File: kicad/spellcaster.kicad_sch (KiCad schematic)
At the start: 38 parts, among them SW1 SW_Push, SW2 SW_Push, U1 nRF52820-QDxx, Y1 32k, Y2 Crystal_GND24

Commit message: Initial routing
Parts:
- removed H3, H4: MountingHole, MountingHole:MountingHole_2.2mm_M2_Pad_Via, symbol Mechanical:MountingHole
- removed SW1, SW2: SW_Push, Button_Switch_SMD:SW_SPST_PTS645, symbol Switch:SW_Push
- added C14, C16: 100n, Capacitor_SMD:C_0402_1005Metric, symbol Device:C_Small
- added R2, R3: 10k, Resistor_SMD:R_0402_1005Metric, symbol Device:R_Small
- added S2: B3U-1000P, Snapeda:SW_B3U-1000P, symbol Snapeda:B3U-1000P
- added U2: LSM6DSL, Package_LGA:LGA-14_3x2.5mm_P0.5mm_LayoutBorder3x4y, symbol Sensor_Motion:LSM6DSL
- BT1: footprint Battery:BatteryHolder_Keystone_3002_1x2032 -> Connector_Wire:SolderWire-0.5sqmm_1x02_P4.8mm_D0.9mm_OD2.3mm
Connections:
- net BTN_A: now also S2.2
- net GND: now also C14.1, C16.1, S2.1, U2.1 (SDO/SA0), U2.2 (SDX), U2.3 (SCX), U2.6 (GND), U2.7 (GND)
- net GPIO: no longer U1.7 (P0.07)
- net VDD: now also R2.2, R3.2, U2.12 (CS)
- net SDA: now reaches U1.14 (P0.14)
- net SDA: now also R2.1, U2.14 (SDA)
- net SCL: now reaches U1.15 (P0.15)
- net SCL: now also R3.1, U2.13 (SCL)
- net INT2: now reaches U1.6 (P0.06)
- net INT2: now also U2.9 (INT2)
- net BTN_B: no longer names the net of U1.36 (AIN0/P0.02)
- new net: C16.2, U2.8 (VDD)
- new net: C14.2, U2.5 (VDDIO)
- new net INT1: U1.7 (P0.07), U2.4 (INT1)
- no-connect marks 15 -> 13
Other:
- moved on the sheet: BT1, C1, C10, C12, C9, H1, H2, S1, TP1, TP2, TP3, TP4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

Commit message: Silkscreen + stitching
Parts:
- removed H1: MountingHole, MountingHole:MountingHole_2.2mm_M2_Pad_Via, symbol Mechanical:MountingHole
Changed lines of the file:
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@@
-    )
-  )
-  (symbol (lib_id "Mechanical:MountingHole") (at 256.54 17.78 0) (unit 1)
-    (in_bom no) (on_board yes) (dnp no) (fields_autoplaced)
-    (property "Reference" "H1" (at 259.08 17.145 0)
-      (effects (font (size 1.27 1.27)) (justify left))
-    )
-    (property "Value" "MountingHole" (at 259.08 19.685 0)
-      (effects (font (size 1.27 1.27)) (justify left))
-    )
-    (property "Footprint" "MountingHole:MountingHole_2.2mm_M2_Pad_Via" (at 256.54 17.78 0)
-      (effects (font (size 1.27 1.27)) hide)
-    )
-    (property "Datasheet" "~" (at 256.54 17.78 0)
-      (effects (font (size 1.27 1.27)) hide)
-    )
-    (instances
-      (project "spellcaster"
-        (path "/bca210d0-b1b0-44be-885f-55d81883bdbb"
-          (reference "H1") (unit 1)
-        )
-      )
     )
   )

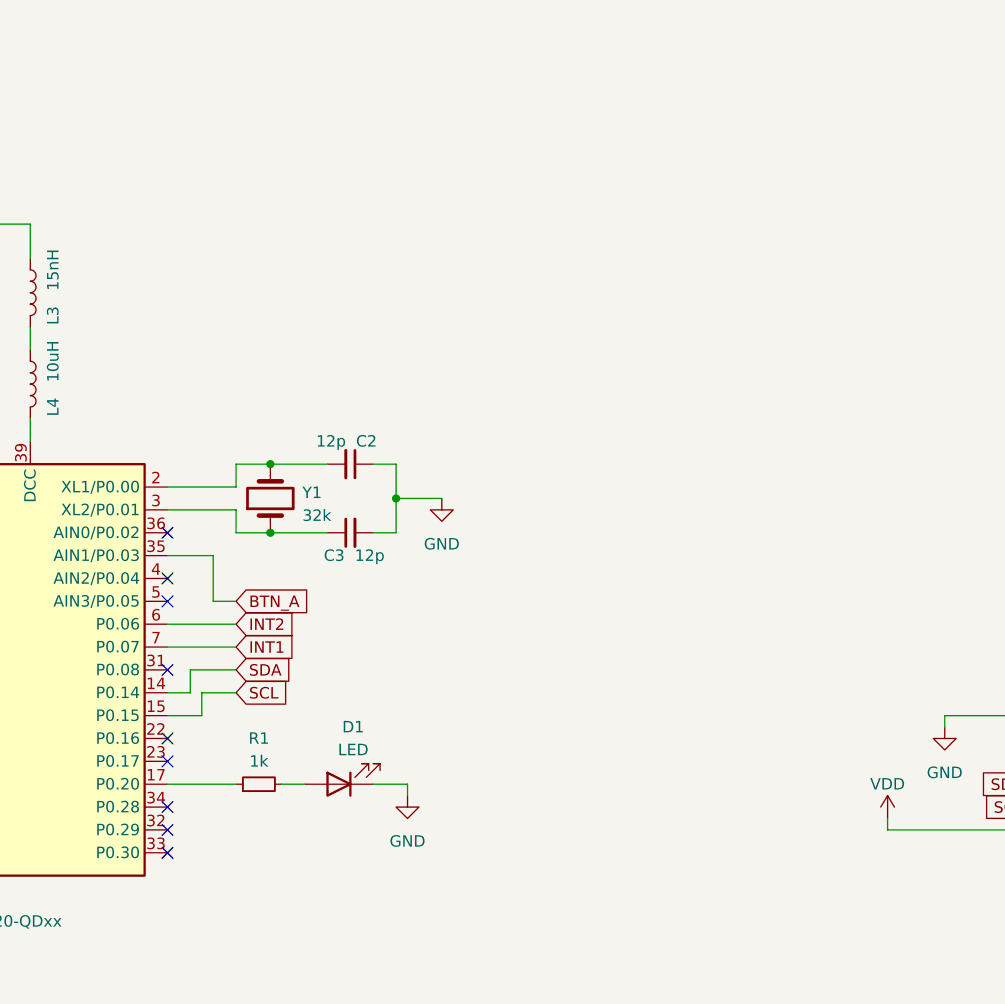
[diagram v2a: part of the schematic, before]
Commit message: Add vibration motor
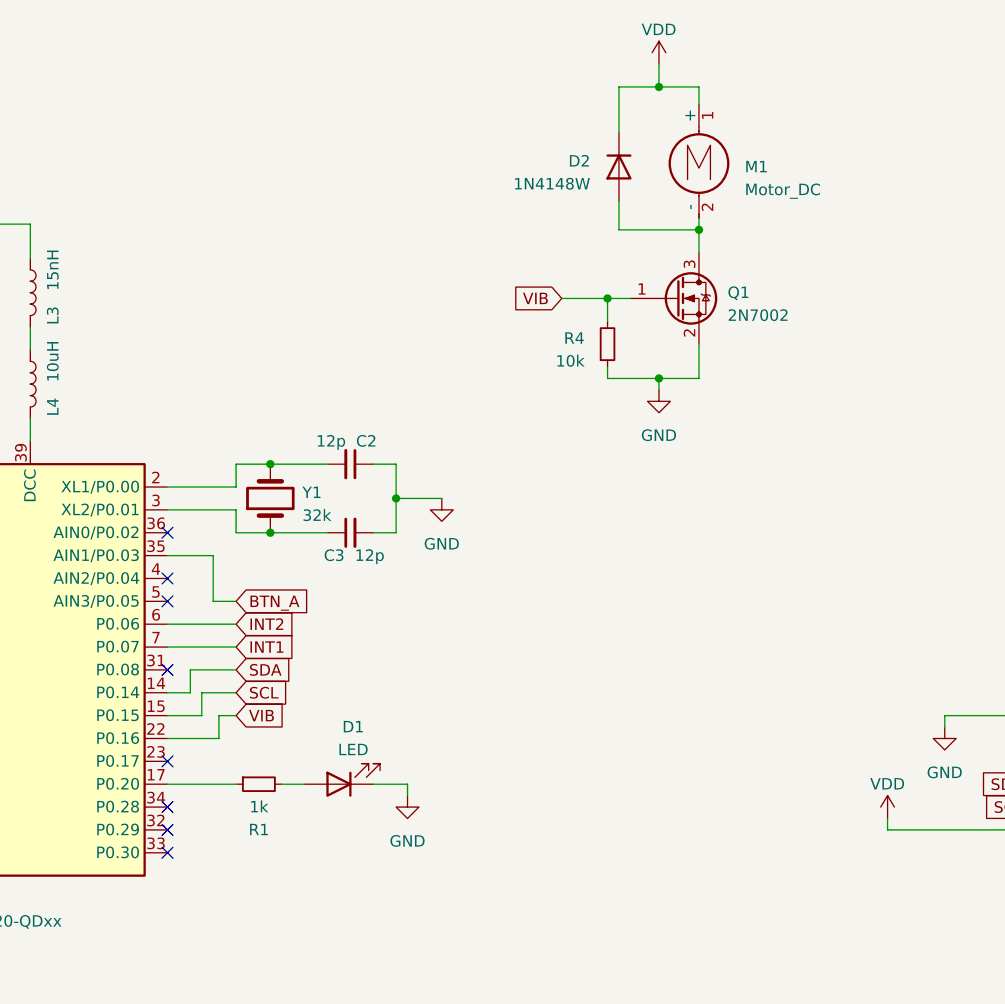
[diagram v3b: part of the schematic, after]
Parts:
- added D2: 1N4148W, Diode_SMD:D_SOD-123, symbol Diode:1N4148W
- added M1: Motor_DC, TestPoint:TestPoint_2Pads_Pitch2.54mm_Drill0.8mm, symbol Motor:Motor_DC
- added Q1: 2N7002, Package_TO_SOT_SMD:SOT-23, symbol Transistor_FET:2N7002
- added R4: 10k, Resistor_SMD:R_0402_1005Metric, symbol Device:R_Small
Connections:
- net GND: now also Q1.2 (S), R4.1
- net VDD: now also D2.1 (K), M1.1 (+)
- net VIB: now reaches U1.22 (P0.16)
- net VIB: now also Q1.1 (G), R4.2
- new net: D2.2 (A), M1.2 (-), Q1.3 (D)
- no-connect marks 13 -> 12

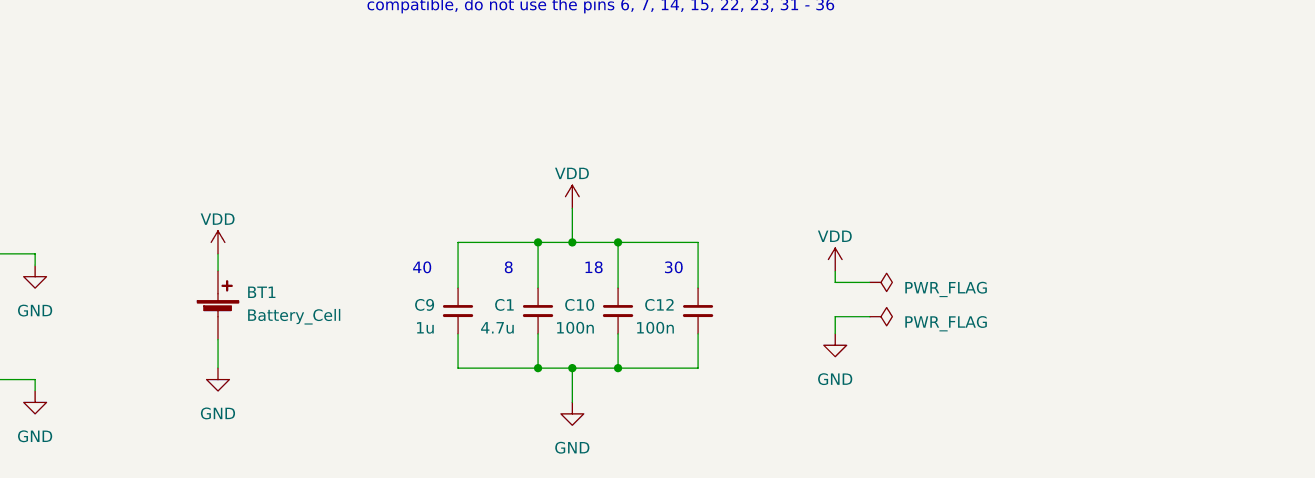
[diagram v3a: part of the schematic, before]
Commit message: Add optional CR2032 holder
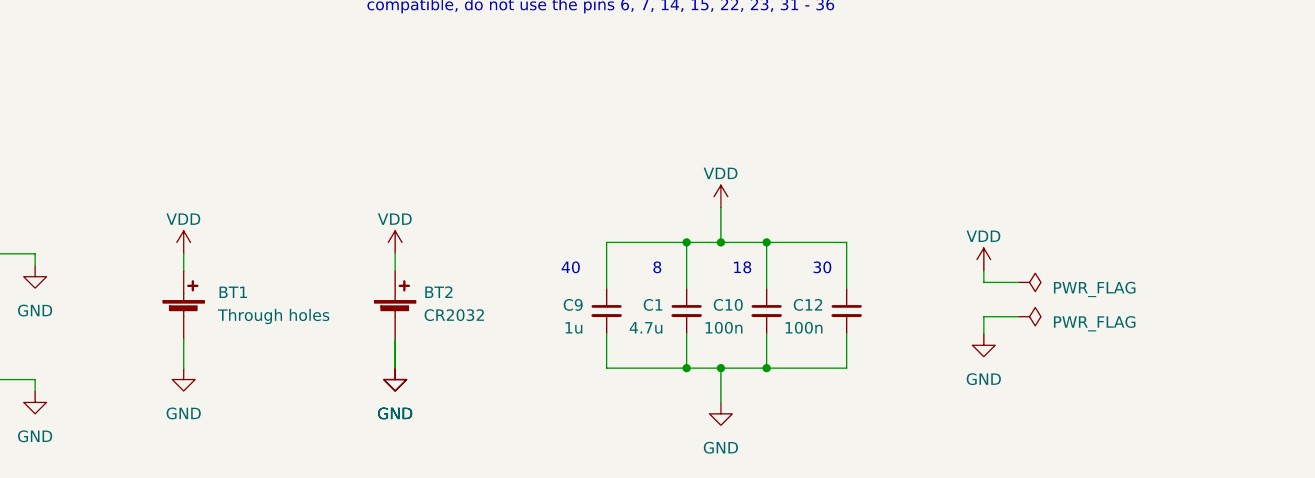
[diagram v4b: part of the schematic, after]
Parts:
- added BT2: CR2032, Battery:BatteryHolder_Keystone_1060_1x2032, symbol Device:Battery_Cell
- BT1: value Battery_Cell -> Through holes
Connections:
- net GND: now also BT2.2 (-)
- net VDD: now also BT2.1 (+)
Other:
- moved on the sheet: BT1, C1, C10, C12, C9

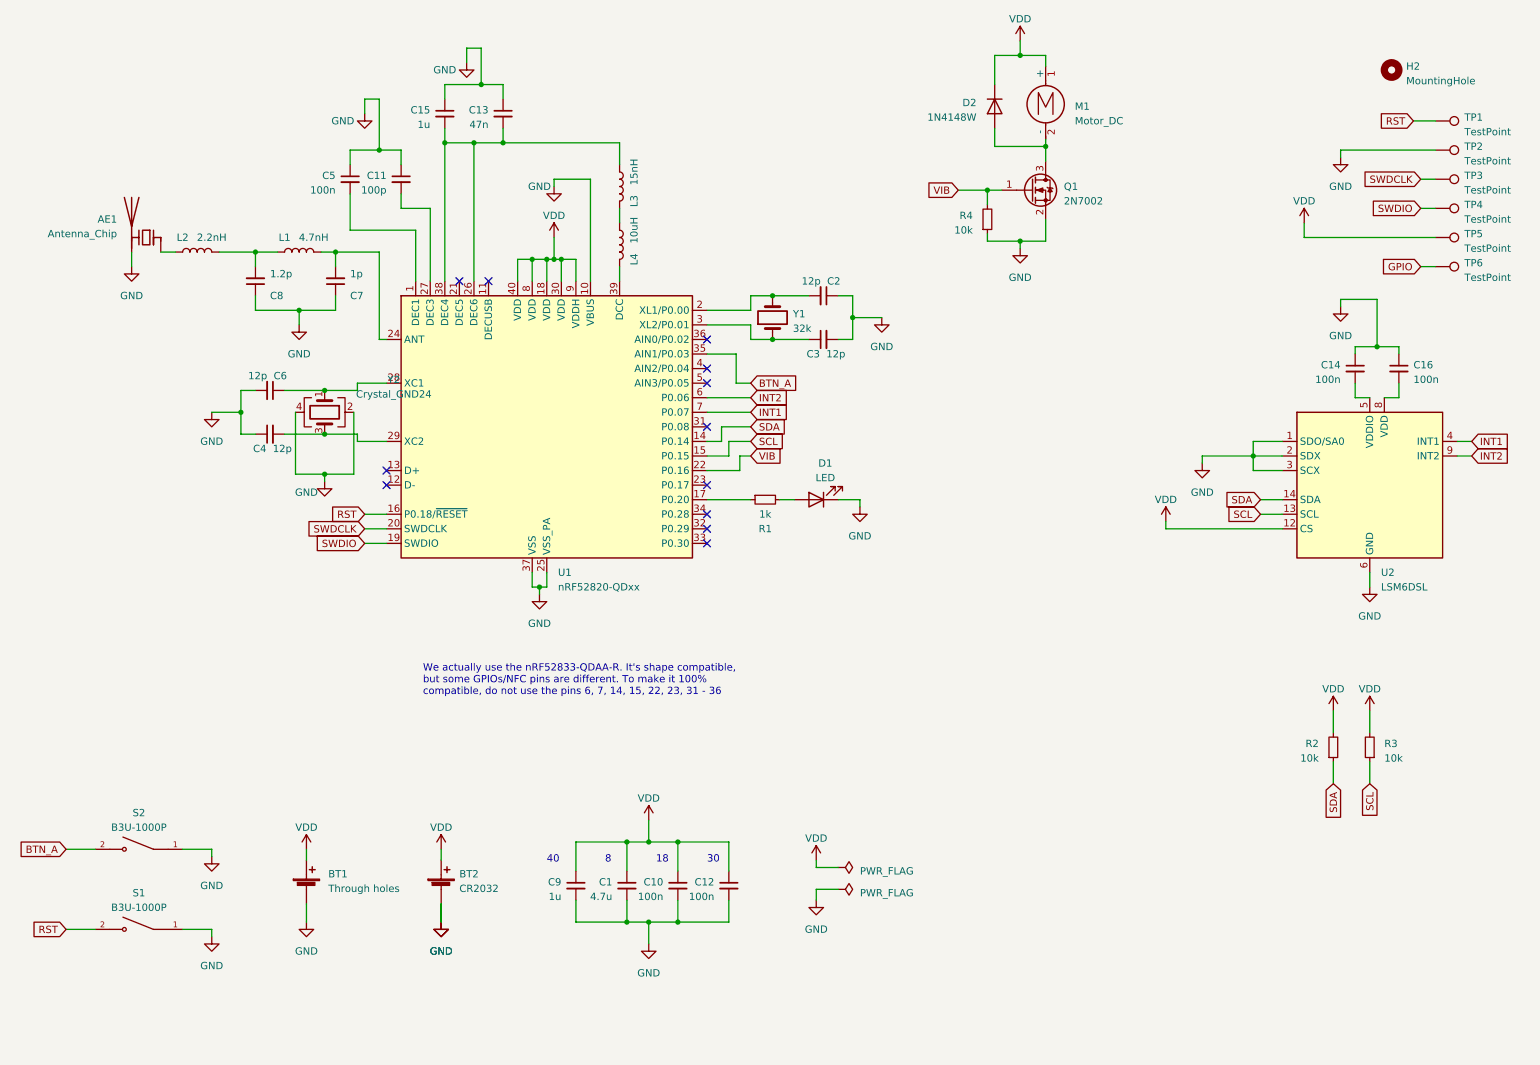
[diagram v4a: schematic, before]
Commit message: Fixed missing accel vcc connection
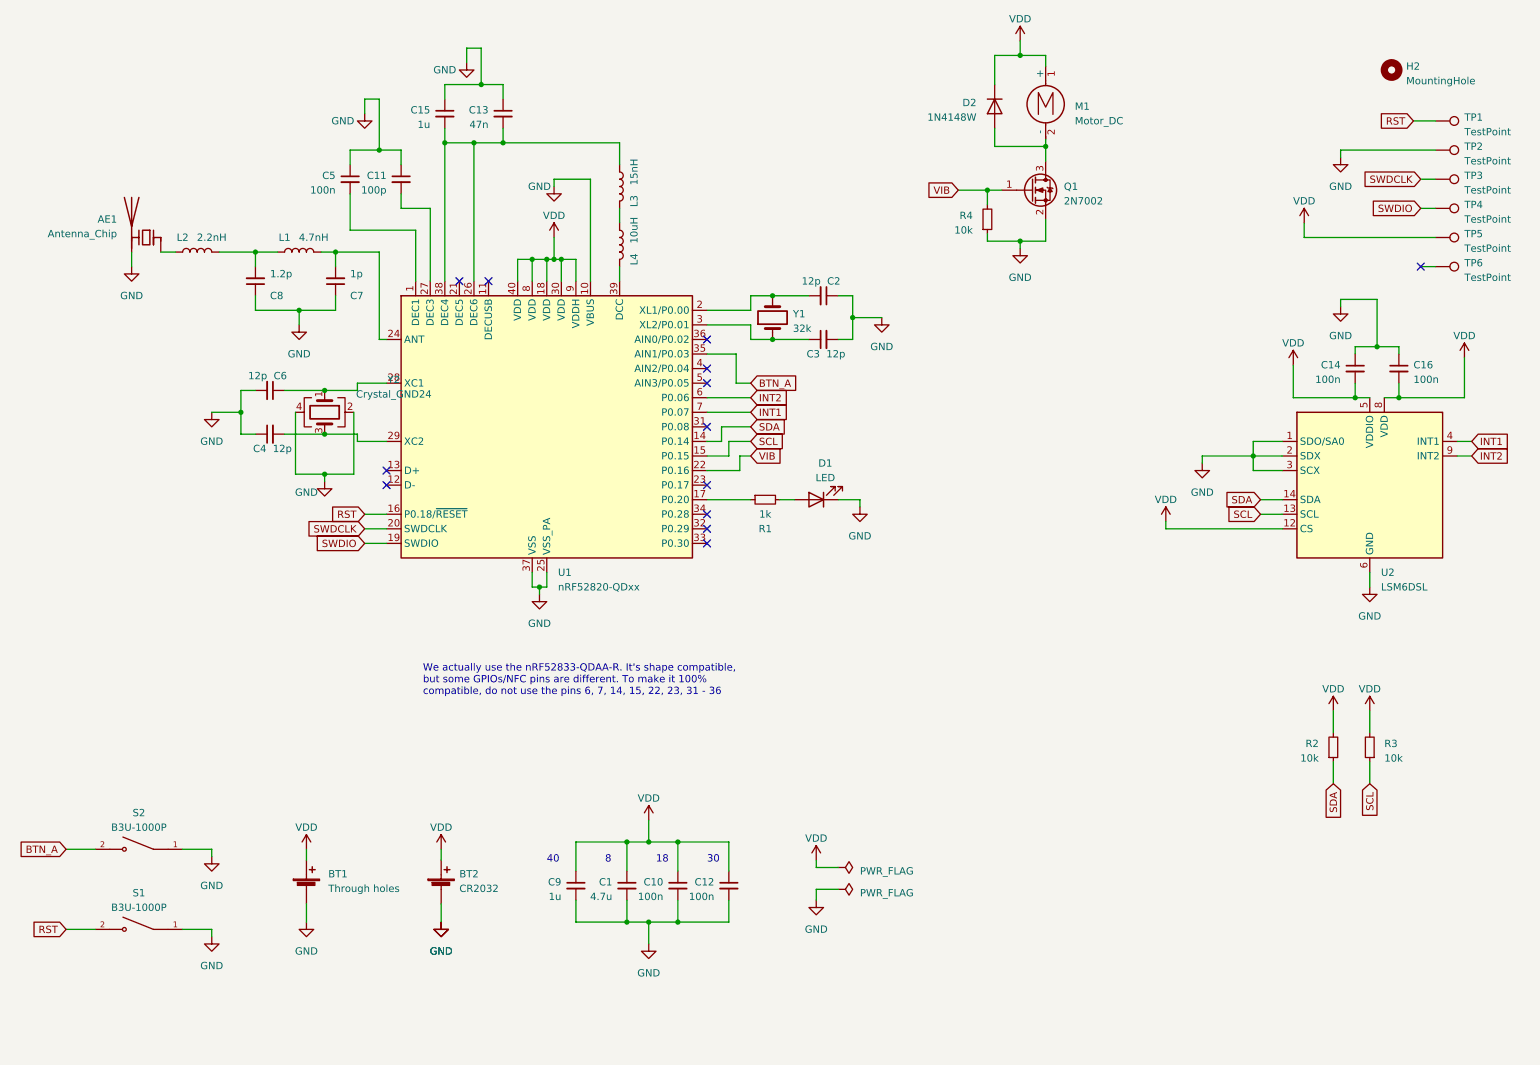
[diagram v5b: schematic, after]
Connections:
- net VDD: now also C14.2, C16.2, U2.5 (VDDIO), U2.8 (VDD)
- net GPIO: no longer names the net of TP6.1
- no-connect marks 12 -> 13
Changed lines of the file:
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@@
   (junction (at 148.59 63.5) (diameter 0) (color 0 0 0 0)
   )
+  (junction (at 250.19 81.28) (diameter 0) (color 0 0 0 0)
+  )
   (junction (at 106.68 57.15) (diameter 0) (color 0 0 0 0)
   )
@@
   (junction (at 254 72.39) (diameter 0) (color 0 0 0 0)
   )
+  (junction (at 257.81 81.28) (diameter 0) (color 0 0 0 0)
+  )
+  (no_connect (at 261.62 58.42))
   (no_connect (at 137.16 78.74))
   (no_connect (at 137.16 104.14))
@@
     (stroke (width 0) (type default))
   )
+  (wire (pts (xy 257.81 81.28) (xy 269.24 81.28))
+    (stroke (width 0) (type default))
+  )
   (wire (pts (xy 148.59 71.12) (xy 154.94 71.12))
     (stroke (width 0) (type default))
@@
     (stroke (width 0) (type default))
   )
+  (wire (pts (xy 239.395 81.28) (xy 250.19 81.28))
+    (stroke (width 0) (type default))
+  )
   (wire (pts (xy 132.08 168.91) (xy 132.08 172.72))
     (stroke (width 0) (type default))
@@
     (stroke (width 0) (type default))
   )
+  (wire (pts (xy 269.24 74.295) (xy 269.24 81.28))
+    (stroke (width 0) (type default))
+  )
   (wire (pts (xy 80.01 71.12) (xy 81.28 71.12))
     (stroke (width 0) (type default))
@@
     (stroke (width 0) (type default))
   )
+  (wire (pts (xy 239.395 75.565) (xy 239.395 81.28))
+    (stroke (width 0) (type default))
+  )
   (wire (pts (xy 77.47 101.6) (xy 81.28 101.6))
     (stroke (width 0) (type default))
   )
   (wire (pts (xy 196.215 50.165) (xy 196.215 53.975))
-    (stroke (width 0) (type default))
-  )
-  (wire (pts (xy 90.805 169.545) (xy 90.805 172.72))
     (stroke (width 0) (type default))
   )
@@
     )
   )
-  (global_label "GPIO" (shape input) (at 261.62 58.42 180) (fields_autoplaced)
-    (effects (font (size 1.27 1.27)) (justify right))
-    (property "Intersheetrefs" "${INTERSHEET_REFS}" (at 254.2389 58.42 0)
-      (effects (font (size 1.27 1.27)) (justify right) hide)
-    )
-  )
   (global_label "VIB" (shape input) (at 180.975 45.085 180) (fields_autoplaced)
     (effects (font (size 1.27 1.27)) (justify right))
@@
         (path "/bca210d0-b1b0-44be-885f-55d81883bdbb"
           (reference "#PWR01") (unit 1)
+        )
+      )
+    )
+  )
+  (symbol (lib_id "power:VDD") (at 239.395 75.565 0) (unit 1)
+    (in_bom yes) (on_board yes) (dnp no) (fields_autoplaced)
+    (property "Reference" "#PWR033" (at 239.395 79.375 0)
+      (effects (font (size 1.27 1.27)) hide)
+    )
+    (property "Value" "VDD" (at 239.395 71.755 0)
+      (effects (font (size 1.27 1.27)))
+    )
+    (property "Footprint" "" (at 239.395 75.565 0)
+      (effects (font (size 1.27 1.27)) hide)
+    )
+    (property "Datasheet" "" (at 239.395 75.565 0)
+      (effects (font (size 1.27 1.27)) hide)
+    )
+    (pin "1")
+    (instances
+      (project "spellcaster"
+        (path "/bca210d0-b1b0-44be-885f-55d81883bdbb"
+          (reference "#PWR033") (unit 1)
         )
       )
@@
         )
       )
+    )
+  )
+  (symbol (lib_id "power:VDD") (at 269.24 74.295 0) (unit 1)
+    (in_bom yes) (on_board yes) (dnp no) (fields_autoplaced)
+    (property "Reference" "#PWR034" (at 269.24 78.105 0)
+      (effects (font (size 1.27 1.27)) hide)
+    )
+    (property "Value" "VDD" (at 269.24 70.485 0)
+      (effects (font (size 1.27 1.27)))
+    )
+    (property "Footprint" "" (at 269.24 74.295 0)
+      (effects (font (size 1.27 1.27)) hide)
+    )
+    (property "Datasheet" "" (at 269.24 74.295 0)
+      (effects (font (size 1.27 1.27)) hide)
+    )
+    (pin "1")
+    (instances
+      (project "spellcaster"
+        (path "/bca210d0-b1b0-44be-885f-55d81883bdbb"
+          (reference "#PWR034") (unit 1)
+        )
+      )

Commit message: Plotted and ordered
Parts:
- M1: now left out of the parts list
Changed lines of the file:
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@@
   )
   (symbol (lib_id "Motor:Motor_DC") (at 196.215 28.575 0) (unit 1)
-    (in_bom yes) (on_board yes) (dnp no) (fields_autoplaced)
+    (in_bom no) (on_board yes) (dnp no) (fields_autoplaced)
     (property "Reference" "M1" (at 201.295 30.48 0)
       (effects (font (size 1.27 1.27)) (justify left))

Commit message: Fixed wrong package for D1
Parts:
- D2: footprint Diode_SMD:D_SOD-123 -> Diode_SMD:D_SOD-323
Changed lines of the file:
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@@
       (effects (font (size 1.27 1.27)) (justify left))
     )
-    (property "Footprint" "Diode_SMD:D_SOD-123" (at 191.77 30.48 0)
+    (property "Footprint" "Diode_SMD:D_SOD-323" (at 191.77 30.48 0)
       (effects (font (size 1.27 1.27)) hide)
     )
